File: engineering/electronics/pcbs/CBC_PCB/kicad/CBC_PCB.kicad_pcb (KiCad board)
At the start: 6 copper layers, 178 x 211 mm, 285 parts, among them J2 AT13-12PB-BM03, J4 AMT0650009DB0000G, J5 AMT0650009DB0000G, J6 AMT0650009DB0000G, J7 AMT0650009DB0000G, Q4 SP015N03BGHTO, U10 CPC1106NTR, U11 CPC1106NTR, U12 74LVC1G17W5-7, U13 74LVC2G02HK3-7, U14 MAX810R, U15 MAX40203AUK+T, U16 1kΩ, U17 1kΩ, U18 1kΩ, U19 1kΩ, U2 2.4GHz, U20 1kΩ, U21 1kΩ, U22 CPC1019NTR, U23 MP9486GN-Z, U25 ADM3053BRWZ-REEL7, U26 ADM3053BRWZ-REEL7, U27 10mΩ, U29 1uF, U30 1uH, U31 1kΩ, U32 1kΩ, U33 MP9486GN-Z, U34 MP9486GN-Z, U35 MP9486GN-Z, U37 MAX40203AUK+T, U38 MAX40203AUK+T, U39 MAX40203AUK+T, U9 120pF, X1 16MHz, X2 16MHz

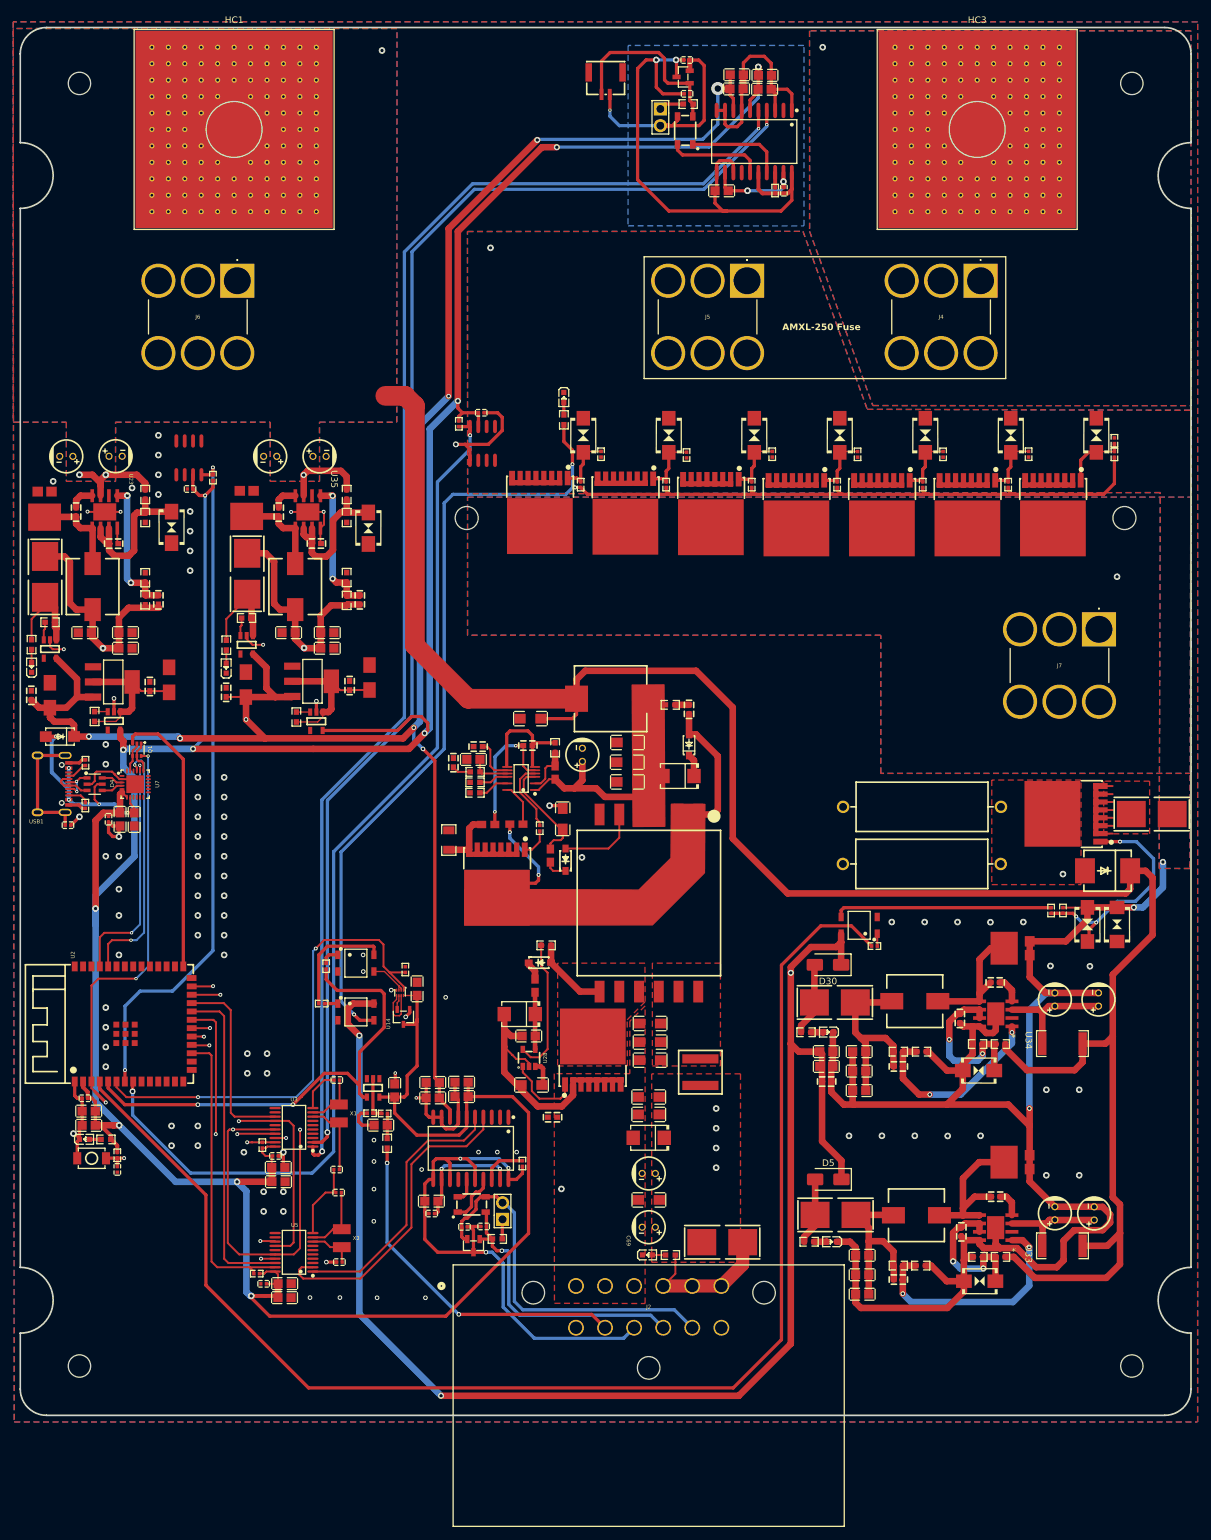
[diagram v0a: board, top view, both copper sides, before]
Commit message: electronics: integrate final CBC PCB routing update
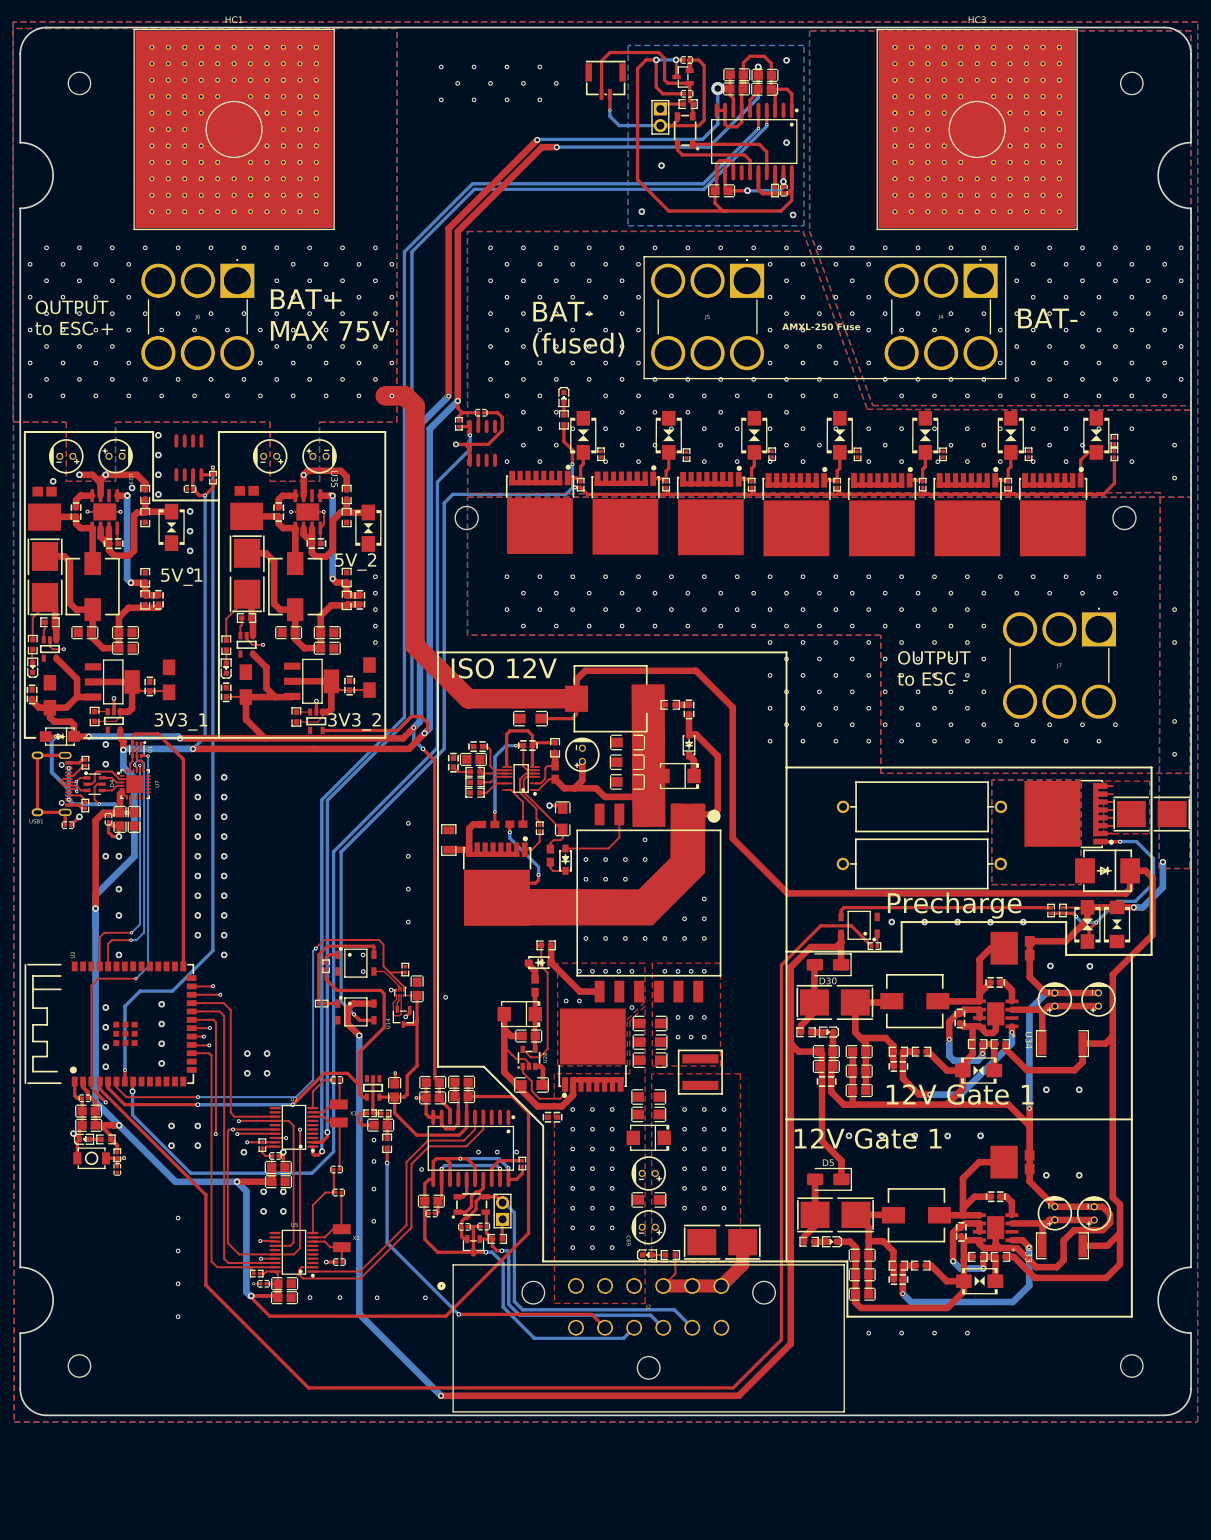
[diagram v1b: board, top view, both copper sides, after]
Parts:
- moved R66 0.18 mm to (62.9, 130.3)
- moved LED5 0.17 mm to (62.9, 133.8)
- moved C44 0.17 mm to (62.8, 137.9)
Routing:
- net GND: track 188.1 -> 189.2 mm, vias 105 -> 285
- net +5V: track 303.1 -> 303.2 mm, vias 8 -> 7
- net Net-(Q2-D): vias 1 -> 0
- net Net-(D19-A): vias 0 -> 8
- net Net-(C71-Pad2): vias 4 -> 18
- net Net-(C66-Pad2): vias 0 -> 10
- net H_PWR-IN--PREFUSE: vias 1 -> 86
- net H_PWR-IN-: vias 4 -> 143
- net H_PWR-IN: vias 4 -> 99
- net GNDE: vias 1 -> 24
- net 12V_GATE_V: vias 3 -> 2
- net +5V_P2: vias 1 -> 0
- net +5V_P1: vias 1 -> 0
- added copper zone on B.Cu, net Net-(Q2-D)
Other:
- board text added: "12V Gate 1"
- board text added: "3V3_1"
- board text added: "3V3_2"
- board text added: "5V_1"
- board text added: "5V_2"
- board text added: "BAT+ MAX 75V"
- board text added: "BAT-"
- board text added: "BAT- (fused)"
- board text added: "ISO 12V"
- board text added: "OUTPUT to ESC +"
- board text added: "OUTPUT to ESC -"
- board text added: "Precharge"
